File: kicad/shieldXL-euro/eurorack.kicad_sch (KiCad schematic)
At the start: 62 parts, among them J101 Eurorack power, J102 IN L, J103 IN R, J104 OUT L, J105 OUT R, J106 MIDI IN, J107 MIDI OUT, J108 DX07S024WJ1R350, J109 USB 1, J110 USB 2, J111 USB 3, J112 Pi USB, inner stack, J113 Pi USB, outer stack, J115 CORONE I/1, J116 CORONE I/2, J117 CORONE O/1, J118 CORONE O/2, J119 CORONE O/3, J120 CORONE O/4, J121 Corone, J122 ii, J123 MIDI OUT A/B, U101 TL074, U102 USBLC6-2SC6, U103 USBLC6-2SC6, U104 USBLC6-2SC6, U105 74LVC1G125

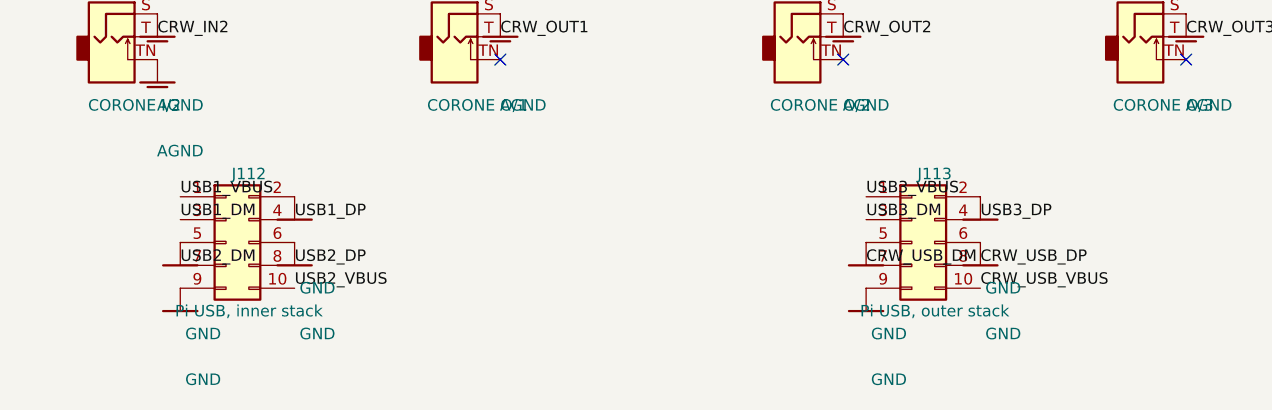
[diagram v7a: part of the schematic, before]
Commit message: Pi USB ribbons: 8-way - boxed 2 x 4 IDC on the main board, plain 2 x 4 header on the adapters
Pinout in ribbon order: VBUS A, GND, D- A, D+ A, GND, D- B, D+ B, VBUS B.
Symbol ids kept, so Update PCB swaps the footprints in place.

Co-Authored-By: Claude Opus 5.5 <noreply@anthropic.com>
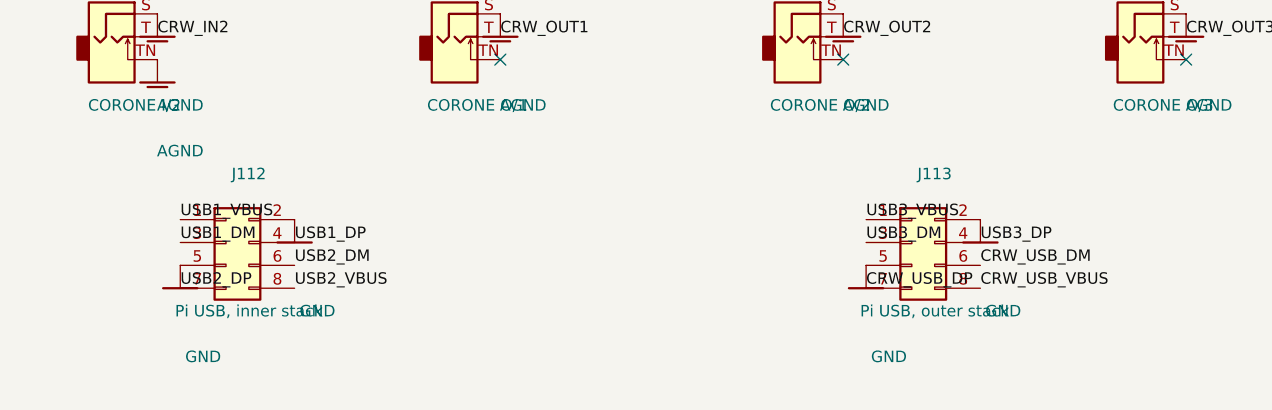
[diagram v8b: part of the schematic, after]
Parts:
- J112, J113: footprint Connector_IDC:IDC-Header_2x05_P2.54mm_Vertical -> Connector_IDC:IDC-Header_2x04_P2.54mm_Vertical; symbol Connector_Generic:Conn_02x05_Odd_Even -> Connector_Generic:Conn_02x04_Odd_Even
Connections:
- net CRW_USB_DM: now also J113.6 (Pin_6); no longer J113.7 (Pin_7)
- net CRW_USB_DP: now also J113.7 (Pin_7); no longer J113.8 (Pin_8)
- net CRW_USB_VBUS: now also J113.8 (Pin_8); no longer J113.10 (Pin_10)
- net GND: no longer J112.6 (Pin_6), J112.9 (Pin_9), J113.6 (Pin_6), J113.9 (Pin_9)
- net USB2_DM: now also J112.6 (Pin_6); no longer J112.7 (Pin_7)
- net USB2_DP: now also J112.7 (Pin_7); no longer J112.8 (Pin_8)
- net USB2_VBUS: now also J112.8 (Pin_8); no longer J112.10 (Pin_10)
